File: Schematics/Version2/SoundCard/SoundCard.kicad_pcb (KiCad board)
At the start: 4 copper layers, 101.6 x 38.4 mm, 46 parts, among them J1 Screw_Terminal_01x03, J2 AudioJack3, J3 Conn, Q1 Q_NJFET_DSG, Q2 Q_NJFET_DSG, Q3 Q_NJFET_DSG, Q4 Q_NJFET_DSG, U1 TL072, U2 MAX505, U3 AS3340, U4 TL072, U5 TL072

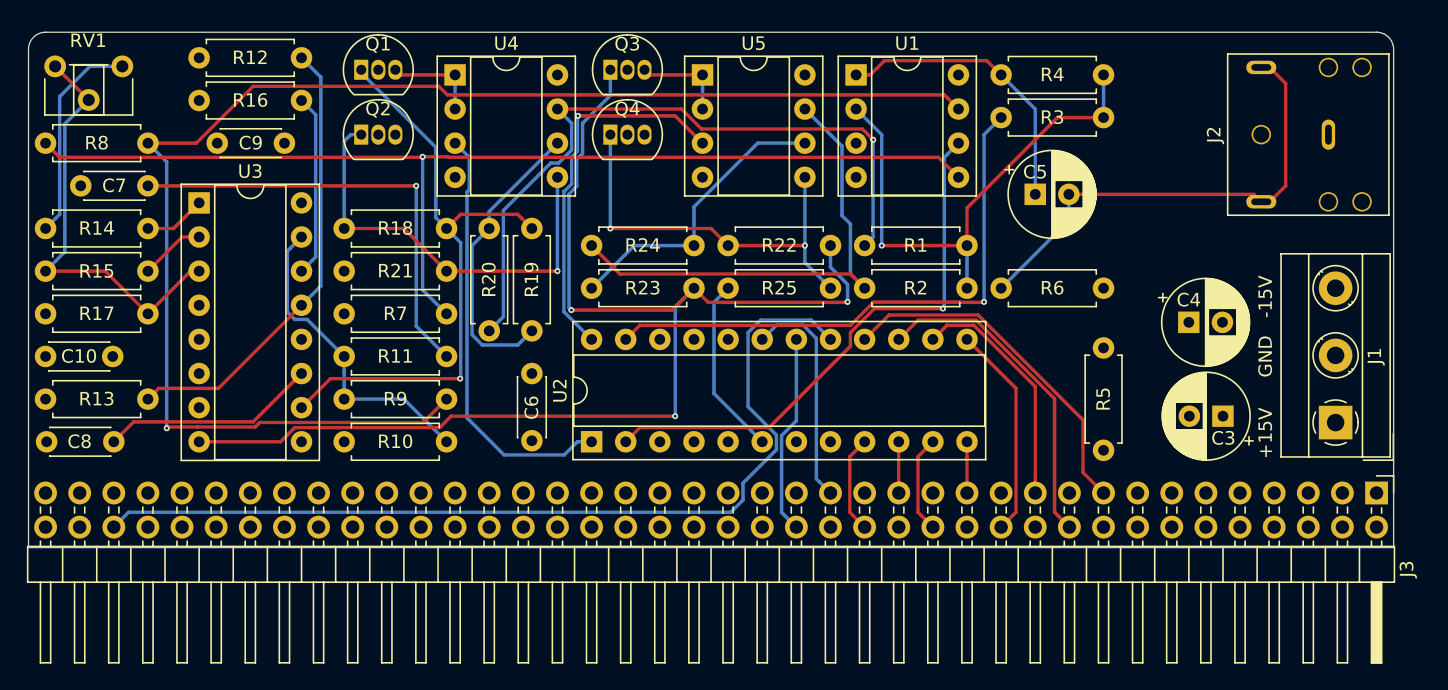
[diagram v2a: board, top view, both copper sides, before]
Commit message: Sound Card: Finish routing SMD PCB for rev 2
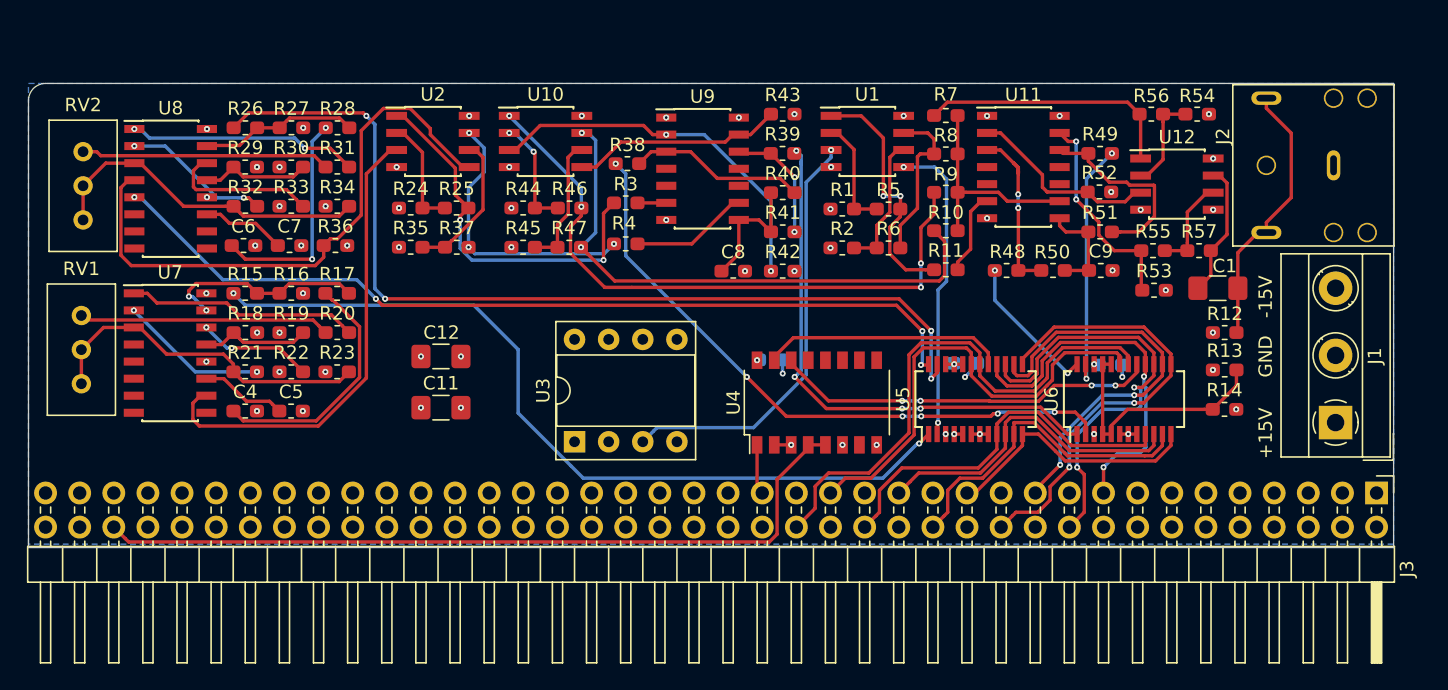
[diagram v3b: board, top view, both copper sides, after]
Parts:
- removed Q1, Q2, Q3, Q4: Q_NJFET_DSG, Package_TO_SOT_THT:TO-92_Inline
- added C1: 100µF, Capacitor_SMD:C_1206_3216Metric_Pad1.42x1.75mm_HandSolder, F.Cu at (152.0, 118.1)
- added C11: 100µF, Capacitor_SMD:C_1206_3216Metric_Pad1.42x1.75mm_HandSolder, F.Cu at (94.2, 127.0)
- added C12: 100µF, Capacitor_SMD:C_1206_3216Metric_Pad1.42x1.75mm_HandSolder, F.Cu at (94.2, 123.2)
- added C2: 100nF, Capacitor_SMD:C_0603_1608Metric_Pad1.05x0.95mm_HandSolder, B.Cu at (144.0, 123.8)
- added R26: 100kΩ, Resistor_SMD:R_0603_1608Metric_Pad1.05x0.95mm_HandSolder, F.Cu at (79.6, 106.2)
- added R27: 360kΩ, Resistor_SMD:R_0603_1608Metric_Pad1.05x0.95mm_HandSolder, F.Cu at (83.1, 106.2)
- added R28: 470Ω, Resistor_SMD:R_0603_1608Metric_Pad1.05x0.95mm_HandSolder, F.Cu at (86.5, 106.2)
- added R29: 1.5MΩ, Resistor_SMD:R_0603_1608Metric_Pad1.05x0.95mm_HandSolder, F.Cu at (79.6, 109.1)
- added R30: 47Ω, Resistor_SMD:R_0603_1608Metric_Pad1.05x0.95mm_HandSolder, F.Cu at (83.1, 109.1)
- added R31: 24kΩ, Resistor_SMD:R_0603_1608Metric_Pad1.05x0.95mm_HandSolder, F.Cu at (86.5, 109.1)
- added R32: 5.6kΩ, Resistor_SMD:R_0603_1608Metric_Pad1.05x0.95mm_HandSolder, F.Cu at (79.6, 112.0)
- added R33: 1.8kΩ, Resistor_SMD:R_0603_1608Metric_Pad1.05x0.95mm_HandSolder, F.Cu at (83.1, 112.0)
- added R34: 820Ω, Resistor_SMD:R_0603_1608Metric_Pad1.05x0.95mm_HandSolder, F.Cu at (86.5, 112.0)
- added R35: 10kΩ, Resistor_SMD:R_0603_1608Metric_Pad1.05x0.95mm_HandSolder, F.Cu at (91.9, 115.1)
- added R36: 51kΩ, Resistor_SMD:R_0603_1608Metric_Pad1.05x0.95mm_HandSolder, F.Cu at (86.3, 114.9)
- added R37: 2.4kΩ, Resistor_SMD:R_0603_1608Metric_Pad1.05x0.95mm_HandSolder, F.Cu at (95.4, 115.1)
- added R38: 16kΩ, Resistor_SMD:R_0603_1608Metric_Pad1.05x0.95mm_HandSolder, F.Cu at (108.1, 108.8)
- added R39: 16kΩ, Resistor_SMD:R_0603_1608Metric_Pad1.05x0.95mm_HandSolder, F.Cu at (119.6, 108.1)
- added R40: 2.4kΩ, Resistor_SMD:R_0603_1608Metric_Pad1.05x0.95mm_HandSolder, F.Cu at (119.6, 111.0)
- added R41: 2.4kΩ, Resistor_SMD:R_0603_1608Metric_Pad1.05x0.95mm_HandSolder, F.Cu at (119.6, 113.9)
- added R42: 47kΩ, Resistor_SMD:R_0603_1608Metric_Pad1.05x0.95mm_HandSolder, F.Cu at (119.6, 116.8)
- added R43: 47kΩ, Resistor_SMD:R_0603_1608Metric_Pad1.05x0.95mm_HandSolder, F.Cu at (119.6, 105.2)
- added R44: 10kΩ, Resistor_SMD:R_0603_1608Metric_Pad1.05x0.95mm_HandSolder, F.Cu at (100.3, 112.1)
- added R45: 10kΩ, Resistor_SMD:R_0603_1608Metric_Pad1.05x0.95mm_HandSolder, F.Cu at (100.3, 115.1)
- added R46: 20kΩ, Resistor_SMD:R_0603_1608Metric_Pad1.05x0.95mm_HandSolder, F.Cu at (103.8, 112.1)
- added R47: 20kΩ, Resistor_SMD:R_0603_1608Metric_Pad1.05x0.95mm_HandSolder, F.Cu at (103.7, 115.1)
- added R48: 16kΩ, Resistor_SMD:R_0603_1608Metric_Pad1.05x0.95mm_HandSolder, F.Cu at (136.3, 116.8)
- added R49: 16kΩ, Resistor_SMD:R_0603_1608Metric_Pad1.05x0.95mm_HandSolder, F.Cu at (143.3, 108.1)
- added R50: 2.4kΩ, Resistor_SMD:R_0603_1608Metric_Pad1.05x0.95mm_HandSolder, F.Cu at (139.8, 116.8)
- added R51: 2.4kΩ, Resistor_SMD:R_0603_1608Metric_Pad1.05x0.95mm_HandSolder, F.Cu at (143.3, 113.9)
- added R52: 47kΩ, Resistor_SMD:R_0603_1608Metric_Pad1.05x0.95mm_HandSolder, F.Cu at (143.2, 110.9)
- added R53: 47kΩ, Resistor_SMD:R_0603_1608Metric_Pad1.05x0.95mm_HandSolder, F.Cu at (147.3, 118.3)
- added R54: 10kΩ, Resistor_SMD:R_0603_1608Metric_Pad1.05x0.95mm_HandSolder, F.Cu at (150.5, 105.2)
- added R55: 10kΩ, Resistor_SMD:R_0603_1608Metric_Pad1.05x0.95mm_HandSolder, F.Cu at (147.2, 115.3)
- added R56: 20kΩ, Resistor_SMD:R_0603_1608Metric_Pad1.05x0.95mm_HandSolder, F.Cu at (147.1, 105.2)
- added R57: 4.7kΩ, Resistor_SMD:R_0603_1608Metric_Pad1.05x0.95mm_HandSolder, F.Cu at (150.6, 115.3)
- added RV2: 10k, Potentiometer_THT:Potentiometer_Bourns_3386C_Horizontal, F.Cu at (67.6, 108.0)
- added U10: TL072, Package_SO:SOIC-8_3.9x4.9mm_P1.27mm, F.Cu at (102.0, 107.2)
- added U11: AS3360, Package_SO:SOIC-14_3.9x8.7mm_P1.27mm, F.Cu at (137.5, 109.1)
- added U12: TL072, Package_SO:SOIC-8_3.9x4.9mm_P1.27mm, F.Cu at (149.0, 110.4)
- added U6: MAX505, Package_SO:SSOP-24_3.9x8.7mm_P0.635mm, F.Cu at (145.0, 126.4)
- added U7: AS3340, Package_SO:SOIC-16_3.9x9.9mm_P1.27mm, F.Cu at (74.0, 122.9)
- added U8: AS3340, Package_SO:SOIC-16_3.9x9.9mm_P1.27mm, F.Cu at (74.1, 110.7)
- added U9: AS3360, Package_SO:SOIC-14_3.9x8.7mm_P1.27mm, F.Cu at (113.7, 109.2)
- C10: footprint Capacitor_THT:C_Disc_D4.3mm_W1.9mm_P5.00mm -> Capacitor_SMD:C_0603_1608Metric_Pad1.05x0.95mm_HandSolder; moved to B.Cu
- C3: value 100µF -> 100nF; footprint Capacitor_THT:CP_Radial_D6.3mm_P2.50mm -> Capacitor_SMD:C_0603_1608Metric_Pad1.05x0.95mm_HandSolder; moved to B.Cu
- C4: value 100µF -> 10nF; footprint Capacitor_THT:CP_Radial_D6.3mm_P2.50mm -> Capacitor_SMD:C_0603_1608Metric_Pad1.05x0.95mm_HandSolder
- C5: value 100µF -> 1nF; footprint Capacitor_THT:CP_Radial_D6.3mm_P2.50mm -> Capacitor_SMD:C_0603_1608Metric_Pad1.05x0.95mm_HandSolder
- C6: value 100nF -> 10nF; footprint Capacitor_THT:C_Disc_D4.3mm_W1.9mm_P5.00mm -> Capacitor_SMD:C_0603_1608Metric_Pad1.05x0.95mm_HandSolder
- C7: value 10nF -> 1nF; footprint Capacitor_THT:C_Disc_D4.3mm_W1.9mm_P5.00mm -> Capacitor_SMD:C_0603_1608Metric_Pad1.05x0.95mm_HandSolder
- C8: value 0.1µF -> 5nF; footprint Capacitor_THT:C_Disc_D4.3mm_W1.9mm_P5.00mm -> Capacitor_SMD:C_0603_1608Metric_Pad1.05x0.95mm_HandSolder
- C9: value 100nF -> 5nF; footprint Capacitor_THT:C_Disc_D4.3mm_W1.9mm_P5.00mm -> Capacitor_SMD:C_0603_1608Metric_Pad1.05x0.95mm_HandSolder
- R1, R24: footprint Resistor_THT:R_Axial_DIN0207_L6.3mm_D2.5mm_P7.62mm_Horizontal -> Resistor_SMD:R_0603_1608Metric_Pad1.05x0.95mm_HandSolder
- R10: value 360kΩ -> 47kΩ; footprint Resistor_THT:R_Axial_DIN0207_L6.3mm_D2.5mm_P7.62mm_Horizontal -> Resistor_SMD:R_0603_1608Metric_Pad1.05x0.95mm_HandSolder
- R11: value 470Ω -> 47kΩ; footprint Resistor_THT:R_Axial_DIN0207_L6.3mm_D2.5mm_P7.62mm_Horizontal -> Resistor_SMD:R_0603_1608Metric_Pad1.05x0.95mm_HandSolder
- R12: value 1.5MΩ -> 100kΩ; footprint Resistor_THT:R_Axial_DIN0207_L6.3mm_D2.5mm_P7.62mm_Horizontal -> Resistor_SMD:R_0603_1608Metric_Pad1.05x0.95mm_HandSolder
- R13: value 47Ω -> 10kΩ; footprint Resistor_THT:R_Axial_DIN0207_L6.3mm_D2.5mm_P7.62mm_Horizontal -> Resistor_SMD:R_0603_1608Metric_Pad1.05x0.95mm_HandSolder
- R14: value 22kΩ -> 6.8kΩ; footprint Resistor_THT:R_Axial_DIN0207_L6.3mm_D2.5mm_P7.62mm_Horizontal -> Resistor_SMD:R_0603_1608Metric_Pad1.05x0.95mm_HandSolder
- R15: value 5.6kΩ -> 100kΩ; footprint Resistor_THT:R_Axial_DIN0207_L6.3mm_D2.5mm_P7.62mm_Horizontal -> Resistor_SMD:R_0603_1608Metric_Pad1.05x0.95mm_HandSolder
- R16: value 1.5kΩ -> 360kΩ; footprint Resistor_THT:R_Axial_DIN0207_L6.3mm_D2.5mm_P7.62mm_Horizontal -> Resistor_SMD:R_0603_1608Metric_Pad1.05x0.95mm_HandSolder
- R17: value 820Ω -> 470Ω; footprint Resistor_THT:R_Axial_DIN0207_L6.3mm_D2.5mm_P7.62mm_Horizontal -> Resistor_SMD:R_0603_1608Metric_Pad1.05x0.95mm_HandSolder
- R18: value 10kΩ -> 1.5MΩ; footprint Resistor_THT:R_Axial_DIN0207_L6.3mm_D2.5mm_P7.62mm_Horizontal -> Resistor_SMD:R_0603_1608Metric_Pad1.05x0.95mm_HandSolder
- R19: value 10kΩ -> 47Ω; footprint Resistor_THT:R_Axial_DIN0207_L6.3mm_D2.5mm_P7.62mm_Horizontal -> Resistor_SMD:R_0603_1608Metric_Pad1.05x0.95mm_HandSolder
- R2: value 22kΩ -> 10kΩ; footprint Resistor_THT:R_Axial_DIN0207_L6.3mm_D2.5mm_P7.62mm_Horizontal -> Resistor_SMD:R_0603_1608Metric_Pad1.05x0.95mm_HandSolder
- R20: value 10kΩ -> 24kΩ; footprint Resistor_THT:R_Axial_DIN0207_L6.3mm_D2.5mm_P7.62mm_Horizontal -> Resistor_SMD:R_0603_1608Metric_Pad1.05x0.95mm_HandSolder
- R21: value 10kΩ -> 5.6kΩ; footprint Resistor_THT:R_Axial_DIN0207_L6.3mm_D2.5mm_P7.62mm_Horizontal -> Resistor_SMD:R_0603_1608Metric_Pad1.05x0.95mm_HandSolder
- R22: value 10kΩ -> 1.8kΩ; footprint Resistor_THT:R_Axial_DIN0207_L6.3mm_D2.5mm_P7.62mm_Horizontal -> Resistor_SMD:R_0603_1608Metric_Pad1.05x0.95mm_HandSolder
- R23: value 10kΩ -> 820Ω; footprint Resistor_THT:R_Axial_DIN0207_L6.3mm_D2.5mm_P7.62mm_Horizontal -> Resistor_SMD:R_0603_1608Metric_Pad1.05x0.95mm_HandSolder
- R25: value 10kΩ -> 20kΩ; footprint Resistor_THT:R_Axial_DIN0207_L6.3mm_D2.5mm_P7.62mm_Horizontal -> Resistor_SMD:R_0603_1608Metric_Pad1.05x0.95mm_HandSolder
- R3: value 10kΩ -> 47kΩ; footprint Resistor_THT:R_Axial_DIN0207_L6.3mm_D2.5mm_P7.62mm_Horizontal -> Resistor_SMD:R_0603_1608Metric_Pad1.05x0.95mm_HandSolder
- R4, R7: value 1kΩ -> 47kΩ; footprint Resistor_THT:R_Axial_DIN0207_L6.3mm_D2.5mm_P7.62mm_Horizontal -> Resistor_SMD:R_0603_1608Metric_Pad1.05x0.95mm_HandSolder
- R5: value 100 -> 20kΩ; footprint Resistor_THT:R_Axial_DIN0207_L6.3mm_D2.5mm_P7.62mm_Horizontal -> Resistor_SMD:R_0603_1608Metric_Pad1.05x0.95mm_HandSolder
- R6: value 100kΩ -> 20kΩ; footprint Resistor_THT:R_Axial_DIN0207_L6.3mm_D2.5mm_P7.62mm_Horizontal -> Resistor_SMD:R_0603_1608Metric_Pad1.05x0.95mm_HandSolder
- R8: value 1.5kΩ -> 47kΩ; footprint Resistor_THT:R_Axial_DIN0207_L6.3mm_D2.5mm_P7.62mm_Horizontal -> Resistor_SMD:R_0603_1608Metric_Pad1.05x0.95mm_HandSolder
- R9: value 100kΩ -> 47kΩ; footprint Resistor_THT:R_Axial_DIN0207_L6.3mm_D2.5mm_P7.62mm_Horizontal -> Resistor_SMD:R_0603_1608Metric_Pad1.05x0.95mm_HandSolder
- RV1: footprint Potentiometer_THT:Potentiometer_ACP_CA6-H2,5_Horizontal -> Potentiometer_THT:Potentiometer_Bourns_3386C_Horizontal
- U1: footprint Package_DIP:DIP-8_W7.62mm_Socket -> Package_SO:SOIC-8_3.9x4.9mm_P1.27mm
- U2: value MAX505 -> TL072; footprint Package_DIP:DIP-24_W7.62mm_Socket -> Package_SO:SOIC-8_3.9x4.9mm_P1.27mm
- U3: value AS3340 -> PIC12F675-IP; footprint Package_DIP:DIP-16_W7.62mm_Socket -> Package_DIP:DIP-8_W7.62mm_Socket
- U4: value TL072 -> 74AHCT138; footprint Package_DIP:DIP-8_W7.62mm_Socket -> Package_SO:SOP-16_4.4x10.4mm_P1.27mm
- U5: value TL072 -> MAX505; footprint Package_DIP:DIP-8_W7.62mm_Socket -> Package_SO:SSOP-24_3.9x8.7mm_P0.635mm
- moved R14 88.8 mm to (152.5, 127.1)
- moved R13 87.8 mm to (152.5, 124.2)
- moved R12 71.7 mm to (152.5, 121.4)
- moved C4 70.5 mm to (79.6, 127.3)
- moved C9 61.5 mm to (143.3, 116.8), turned to 0 degrees
- moved R8 59.4 mm to (131.8, 108.1)
- moved C5 57.7 mm to (83.0, 127.3)
- moved C10 54.0 mm to (118.7, 123.4)
- moved C8 47.8 mm to (116.0, 116.8), turned to 0 degrees
- moved R10 40.3 mm to (131.8, 113.8)
- moved R9 40.2 mm to (131.8, 111.0)
- moved R7 40.0 mm to (131.8, 105.3)
- moved R11 37.7 mm to (131.8, 116.7), turned to 0 degrees
- moved U4 36.3 mm to (122.2, 126.6), turned to 90 degrees
- moved R22 33.8 mm to (83.1, 124.3)
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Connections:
- C10 pad 1: -15V -> VCC
- C10 pad 2: GNDA -> GND
- C3 pad 1: +15V -> VCC
- C3 pad 2: GNDA -> GND
- C4 pad 1: GNDA -> Net-(C4-Pad1)
- C4 pad 2: -15V -> GND
- C5 pad 2: Net-(C5-Pad2) -> GND
- C6 pad 1: VCC -> Net-(C6-Pad1)
- C7 pad 2: GNDA -> GND
- C8 pad 2: GNDA -> GND
- C9 pad 1: +15V -> Net-(C9-Pad1)
- C9 pad 2: GNDA -> GND
- J1 pad 2: GNDA -> GND
- J2 pad R: Net-(C5-Pad2) -> Net-(C1-Pad2)
- J2 pad S: GNDA -> GND
- J2 pad T: Net-(C5-Pad2) -> Net-(C1-Pad2)
- J3 pad 37: (no net) -> /Connector/AddressBus2
- R1 pad 1: /VCA1/OUT -> GND
- R10 pad 1: Net-(R10-Pad1) -> /VCA2/VIN2
- R10 pad 2: +15V -> /VCA/VOUT2
- R11 pad 1: Net-(C7-Pad1) -> Net-(R11-Pad1)
- R11 pad 2: Net-(R10-Pad1) -> /VCA2/VIN1
- R12 pad 1: Net-(R12-Pad1) -> Net-(C1-Pad2)
- R12 pad 2: +15V -> GND
- R13 pad 1: GNDA -> VCC
- R13 pad 2: Net-(R12-Pad1) -> Net-(R13-Pad2)
- R14 pad 1: Net-(R14-Pad1) -> Net-(R13-Pad2)
- R14 pad 2: Net-(R14-Pad2) -> GND
- R15 pad 1: Net-(R15-Pad1) -> /VCO-Triangle/CV
- R16 pad 1: GNDA -> Net-(R15-Pad2)
- R16 pad 2: Net-(R16-Pad2) -> +15V
- R17 pad 1: -15V -> Net-(C4-Pad1)
- R17 pad 2: Net-(R15-Pad1) -> Net-(R15-Pad2)
- R18 pad 1: Net-(Q2-Pad1) -> Net-(R18-Pad1)
- R18 pad 2: /VCA1/IN -> +15V
- R19 pad 1: Net-(R19-Pad1) -> GND
- R19 pad 2: /VCA1/IN -> Net-(R18-Pad1)
- R2 pad 1: /VCA2/OUT -> GND
- R2 pad 2: Net-(R1-Pad2) -> Net-(R2-Pad2)
- R20 pad 1: /VCA1/OUT -> Net-(R20-Pad1)
- R20 pad 2: Net-(R19-Pad1) -> Net-(R20-Pad2)
- R21 pad 1: GNDA -> Net-(R21-Pad1)
- R21 pad 2: Net-(Q2-Pad1) -> Net-(R21-Pad2)
- R22 pad 1: Net-(Q4-Pad1) -> GND
- R22 pad 2: /VCA2/IN -> Net-(R22-Pad2)
- R23 pad 1: Net-(R23-Pad1) -> -15V
- R23 pad 2: /VCA2/IN -> Net-(R21-Pad1)
- R24 pad 1: /VCA2/OUT -> GND
- R24 pad 2: Net-(R23-Pad1) -> Net-(R24-Pad2)
- R25 pad 1: GNDA -> Net-(R24-Pad2)
- R25 pad 2: Net-(Q4-Pad1) -> /VCO-Triangle/TriangleOut
- R3 pad 1: /DAC/VOUTD -> /VCA/VIN1
- R3 pad 2: Net-(R1-Pad2) -> /VCO-Triangle/TriangleOut
- R4 pad 1: Net-(C5-Pad1) -> /VCA/VIN2
- R4 pad 2: Net-(R1-Pad2) -> /VCO-Pulse/PulseOut
- R5 pad 1: GND -> Net-(R1-Pad2)
- R5 pad 2: GNDA -> Net-(R11-Pad1)
- R6 pad 1: Net-(C5-Pad2) -> Net-(R2-Pad2)
- R6 pad 2: GNDA -> Net-(R6-Pad2)
- R7 pad 1: Net-(R7-Pad1) -> /VCA2/VIN2
- R7 pad 2: GNDA -> /VCA2/VOUT1
- R8 pad 1: Net-(R8-Pad1) -> /VCA2/VIN2
- R8 pad 2: Net-(R7-Pad1) -> Net-(R6-Pad2)
- R9 pad 1: Net-(R8-Pad1) -> /VCA2/VIN2
- R9 pad 2: Net-(R10-Pad1) -> /VCA/VOUT1
- RV1 pad 1: Net-(R14-Pad1) -> Net-(R20-Pad1)
- RV1 pad 2: Net-(R15-Pad1) -> Net-(R21-Pad1)
- RV1 pad 3: Net-(R15-Pad1) -> Net-(R21-Pad1)
- U1 pad 1: Net-(C5-Pad1) -> Net-(R11-Pad1)
- U1 pad 3: GNDA -> Net-(U1-Pad3)
- U1 pad 5: Net-(R7-Pad1) -> /DAC/VOUT0
- U1 pad 6: /VCO/CV -> Net-(R2-Pad2)
- U1 pad 7: Net-(R8-Pad1) -> Net-(R6-Pad2)
- U2 pad 1: /VCA1/CV -> /VCO-Triangle/TriangleOut
- U2 pad 2: /VCO/CV -> Net-(R24-Pad2)
- U2 pad 3: GND -> Net-(U2-Pad3)
- U2 pad 4: VCC -> -15V
- U2 pad 5: VCC -> Net-(R36-Pad1)
- U2 pad 6: GNDA -> Net-(R35-Pad2)
- U2 pad 7: GND -> /VCO-Pulse/PulseOut
- U2 pad 8: GND -> +15V
- U3 pad 1: Net-(R14-Pad2) -> VCC
- U3 pad 2: Net-(R15-Pad2) -> (no net)
- U3 pad 3: Net-(R15-Pad1) -> Net-(U1-Pad3)
- U3 pad 8: /VCA2/IN -> GND
- U4 pad 1: Net-(Q1-Pad3) -> /Connector/AddressBus2
- U4 pad 2: Net-(Q1-Pad3) -> GND
- U4 pad 3: /VCA1/CV -> GND
- U4 pad 4: -15V -> /Connector/~PI
- U4 pad 5: Net-(Q2-Pad1) -> /Connector/~PI
- U4 pad 6: Net-(R19-Pad1) -> VCC
- U4 pad 7: /VCA1/OUT -> (no net)
- U4 pad 8: +15V -> GND
- U5 pad 1: Net-(Q3-Pad3) -> /VCO-Triangle/CV
- U5 pad 2: Net-(Q3-Pad3) -> /DAC/VOUT0
- U5 pad 3: /VCA2/CV -> GND
- U5 pad 4: -15V -> VCC
- U5 pad 5: Net-(Q4-Pad1) -> VCC
- U5 pad 6: Net-(R23-Pad1) -> GND
- U5 pad 7: /VCA2/OUT -> GND
- U5 pad 8: +15V -> GND
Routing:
- net +15V: track 0.00 -> 150.7 mm, vias 0 -> 13
- net VCC: track 0.00 -> 143.2 mm, vias 0 -> 6
- net Net-(R8-Pad1): track 106.3 -> 0.00 mm, vias 1 -> 0
- net /VCA2/IN: track 92.0 -> 0.00 mm, vias 3 -> 0
- net Net-(R7-Pad1): track 81.4 -> 0.00 mm, vias 1 -> 0
- net /VCO-Pulse/FrequencyCV: track 0.00 -> 71.1 mm, vias 0 -> 4
- net /VCO-Pulse/PWMCV: track 0.00 -> 65.9 mm, vias 0 -> 4
- net /VCO-Triangle/CV: track 0.00 -> 61.6 mm, vias 0 -> 2
- net /VCA1/OUT: track 52.4 -> 0.00 mm, vias 1 -> 0
- net /VCA/CV1: track 0.00 -> 47.6 mm, vias 0 -> 6
- net /VCA/VOUT1: track 0.00 -> 47.4 mm, vias 0 -> 4
- net /VCA1/IN: track 46.0 -> 0.00 mm, vias 1 -> 0
- net Net-(R36-Pad1): track 0.00 -> 43.6 mm
- net /DAC/VOUTD: track 42.1 -> 0.00 mm, vias 1 -> 0
- net /VCA/VOUT2: track 0.00 -> 41.6 mm, vias 0 -> 2
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- added copper zone on B.Cu, net GND
- removed copper zone on In2.Cu, net +15V
- removed copper zone on In2.Cu, net -15V
- removed copper zone on In1.Cu, net GNDA
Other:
- board size 101.6 x 38.4 mm -> 101.6 x 34.5 mm
- net class Default: trace_width 0.254 -> 0.127
- board text added: "Sound Card, Rev 2"
- board text removed: "Sound Card, Rev 1"

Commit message: Sound Card: revision 3 fixes the footprint on the two MAX505s
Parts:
- U5, U6: footprint Package_SO:SSOP-24_3.9x8.7mm_P0.635mm -> Package_SO:SSOP-24_5.3x8.2mm_P0.65mm
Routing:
- net VCC: track 143.2 -> 150.3 mm
- net GND: track 7.12 -> 12.0 mm
- net /Connector/DataBus2: track 30.5 -> 33.6 mm
- net /Connector/DataBus0: track 27.3 -> 30.3 mm
- net /Connector/DataBus1: track 33.0 -> 35.9 mm
- net /VCO-Pulse/FrequencyCV: track 71.1 -> 68.2 mm, vias 4 -> 2
- net /Connector/DataBus4: track 19.6 -> 22.4 mm, vias 0 -> 2
- net /Connector/DataBus3: track 35.4 -> 37.9 mm
- net Net-(R13-Pad2): track 18.8 -> 20.4 mm
- net /Connector/DataBus6: track 24.5 -> 23.0 mm, vias 0 -> 2
- net /VCO-Pulse/PWMCV: track 65.9 -> 64.5 mm, vias 4 -> 2
- net /Connector/DataBus5: track 24.5 -> 23.1 mm, vias 0 -> 2
- net Net-(U4-Pad15): track 18.1 -> 19.3 mm, vias 0 -> 2
- net /VCA/CV2: track 40.5 -> 41.7 mm
- net /Connector/AddressBus1: track 40.1 -> 38.9 mm
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- removed copper zone on B.Cu, net GND
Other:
- board text added: "Sound Card, Rev 3"
- board text removed: "Sound Card, Rev 2"
